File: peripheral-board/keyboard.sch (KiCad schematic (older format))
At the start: 141 parts, among them SW2001 1, SW2002 2, SW2003 3, SW2004 4, SW2005 5, SW2006 6, SW2007 7, SW2008 8, SW2009 9, SW2010 0, SW2011 +, SW2012 ´, SW2013 BKSP, SW2014 TROLL, SW2015 §, SW2016 UP, SW2017 RMB, SW2018 Q, SW2019 W, SW2020 E, SW2021 R, SW2022 T, SW2023 Y, SW2024 U, SW2025 I, SW2026 O, SW2027 P, SW2028 Å, SW2029 ¨, SW2030 RETURN, SW2031 ALT_GR, SW2032 <, SW2033 LEFT, SW2034 MMB, SW2035 A, SW2036 S, SW2037 D, SW2038 F, SW2039 G, SW2040 H, SW2041 J, SW2042 K, SW2043 L, SW2044 Ö, SW2045 Ä, SW2046 ', SW2047 ESC, SW2048 TAB, SW2049 ALT, SW2050 DOWN, SW2051 LMB, SW2052 SHIFT_L, SW2053 Z, SW2054 X, SW2055 C, SW2056 V, SW2057 B, SW2058 N, SW2059 M, SW2060 ,, SW2061 ., SW2062 -, SW2063 SHIFT_R, SW2064 FN_R, SW2065 SPACE, SW2066 FN_L, SW2067 RIGHT, SW2068 CTRL, SW2069 SPACE, U2001 4017, U2002 4017, U2003 74HC00

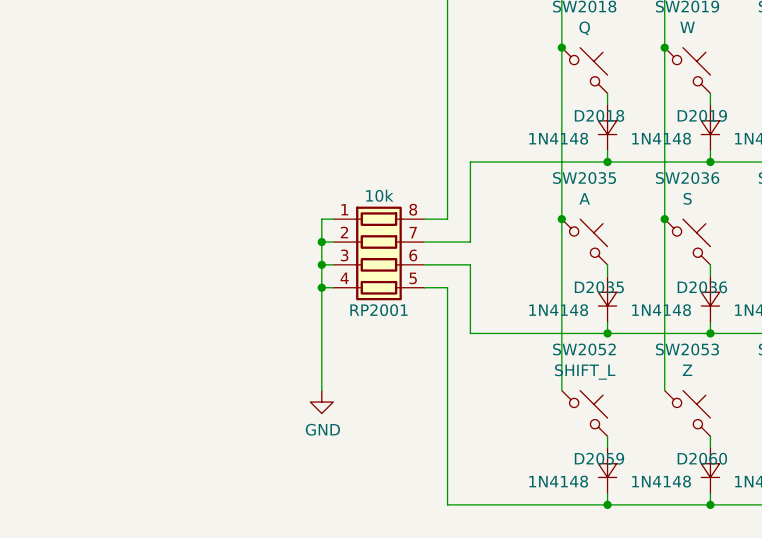
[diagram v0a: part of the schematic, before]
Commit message: connected 3v3 net
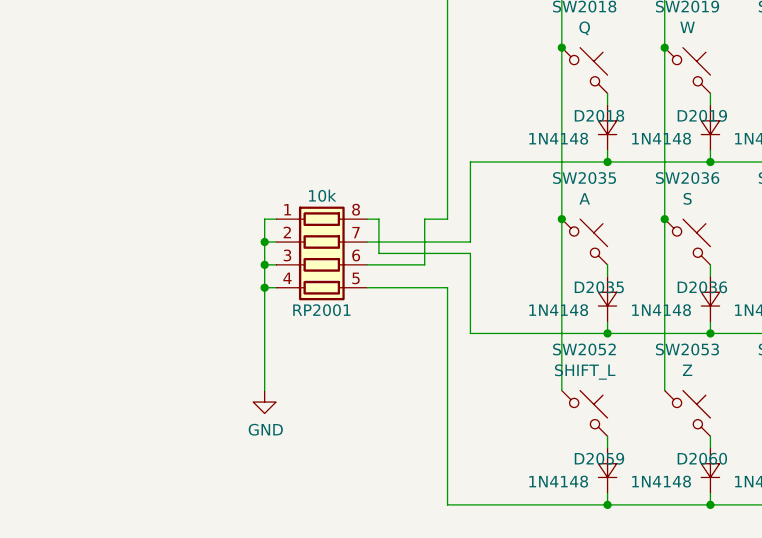
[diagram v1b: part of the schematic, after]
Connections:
- wire segments 236 -> 240
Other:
- moved on the sheet: RP2001
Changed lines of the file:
@@
 L R_Pack04 RP2001
 U 1 1 58209297
-P 2000 5400
-F 0 "RP2001" V 2200 5400 50  0000 C CNN
-F 1 "10k" V 1700 5400 50  0000 C CNN
-F 2 "Resistors_SMD:R_Cat16-4" H 2000 5400 50  0001 C CNN
-F 3 "" H 2000 5400 50  0000 C CNN
-	1    2000 5400
+P 1750 5400
+F 0 "RP2001" V 1950 5400 50  0000 C CNN
+F 1 "10k" V 1450 5400 50  0000 C CNN
+F 2 "Resistors_SMD:R_Cat16-4" H 1750 5400 50  0001 C CNN
+F 3 "" H 1750 5400 50  0000 C CNN
+	1    1750 5400
 	0    1    1    0
 $EndComp
@@
 L GND #PWR030
 U 1 1 5820A281
-P 1750 5950
-F 0 "#PWR030" H 1750 5700 50  0001 C CNN
-F 1 "GND" H 1755 5777 50  0000 C CNN
-F 2 "" H 1750 5950 50  0000 C CNN
-F 3 "" H 1750 5950 50  0000 C CNN
-	1    1750 5950
+P 1500 5950
+F 0 "#PWR030" H 1500 5700 50  0001 C CNN
+F 1 "GND" H 1505 5777 50  0000 C CNN
+F 2 "" H 1500 5950 50  0000 C CNN
+F 3 "" H 1500 5950 50  0000 C CNN
+	1    1500 5950
 	1    0    0    -1
 $EndComp
@@
 Connection ~ 10200 4950
 Connection ~ 10200 4200
-Connection ~ 1750 5500
-Wire Wire Line
-	1800 5500 1750 5500
-Connection ~ 1750 5400
-Wire Wire Line
-	1800 5400 1750 5400
-Connection ~ 1750 5300
-Wire Wire Line
-	1800 5300 1750 5300
-Wire Wire Line
-	1750 5200 1750 5950
-Wire Wire Line
-	1800 5200 1750 5200
+Connection ~ 1500 5500
+Wire Wire Line
+	1550 5500 1500 5500
+Connection ~ 1500 5400
+Wire Wire Line
+	1550 5400 1500 5400
+Connection ~ 1500 5300
+Wire Wire Line
+	1550 5300 1500 5300
+Wire Wire Line
+	1500 5200 1500 5950
+Wire Wire Line
+	1550 5200 1500 5200
 Wire Wire Line
 	2300 5500 2300 6450
 Wire Wire Line
-	2200 5500 2300 5500
-Wire Wire Line
-	2400 5400 2200 5400
-Wire Wire Line
-	2400 5700 2400 5400
-Wire Wire Line
-	2400 5300 2200 5300
-Wire Wire Line
-	2400 4950 2400 5300
+	1950 5500 2300 5500
+Wire Wire Line
+	1950 5300 2400 5300
+Wire Wire Line
+	2400 5300 2400 4950
 Wire Wire Line
 	2300 5200 2200 5200
@@
 Wire Wire Line
 	10200 6350 10200 6450
+Wire Wire Line
+	2000 5200 1950 5200
+Wire Wire Line
+	2000 5350 2400 5350
+Wire Wire Line
+	2000 5350 2000 5200
+Wire Wire Line
+	1950 5400 2200 5400
+Wire Wire Line
+	2200 5400 2200 5200
+Wire Wire Line
+	2400 5350 2400 5700
 $EndSCHEMATC

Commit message: minor fixes
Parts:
- added R2001: 0R, Resistors_SMD:R_1206, symbol R
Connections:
- wire segments 240 -> 241
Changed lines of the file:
@@
 Wire Wire Line
 	7150 1300 7150 1600
-Wire Wire Line
-	6050 1300 7150 1300
 Connection ~ 4300 850
 Wire Wire Line
@@
 Wire Wire Line
 	2400 5350 2400 5700
+$Comp
+L R R2001
+U 1 1 58AA3942
+P 6550 1300
+F 0 "R2001" V 6450 1300 50  0000 C CNN
+F 1 "0R" V 6550 1300 50  0000 C CNN
+F 2 "Resistors_SMD:R_1206" V -70 50  50  0001 C CNN
+F 3 "" H 0   50  50  0001 C CNN
+	1    6550 1300
+	0    1    1    0
+$EndComp
+Wire Wire Line
+	7150 1300 6700 1300
+Wire Wire Line
+	6050 1300 6400 1300
 $EndSCHEMATC

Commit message: peripheral board all done o____O
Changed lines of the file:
@@
 $Descr A4 11693 8268
 encoding utf-8
-Sheet 2 10
+Sheet 2 8
 Title ""
 Date ""
@@
 Text Label 6100 2450 0    60   ~ 0
 COL8
-Text Label 10300 2700 1    60   ~ 0
-COL16
 Text Label 9950 2450 2    60   ~ 0
 COL16
